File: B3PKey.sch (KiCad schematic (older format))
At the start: 4 parts

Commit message: Controller and keyswitch schematic
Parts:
- removed J?: USB_C_Receptacle, symbol Connector:USB_C_Receptacle
- added C?: 1uF, symbol Device:C_Small
- added C? (x3): 0.1uF, symbol Device:C_Small
- added C?: 10uF, symbol Device:C_Small
- added C? (x2): 22pF, symbol Device:C_Small
- added D? (x96): D_Small, symbol Device:D_Small
- added F?: 500mA, symbol Device:Polyfuse_Small
- added MX? (x96): MX-NoLED, symbol MX_Alps_Hybrid:MX-NoLED
- added R? (x2): 10k, symbol Device:R_Small
- added R? (x2): 22, symbol Device:R_Small
- added USB?: Molex-0548190589, symbol random-keyboard-parts:Molex-0548190589
- Y?: value Crystal_GND24_Small -> 16MHz
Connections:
- net D+: now also R?.2, USB?.3 (D+); no longer U?.4 (D+)
- net D-: now also R?.2, USB?.4 (D-); no longer U?.3 (D-)
- net at U?.13 (~RESET): now also SW?.2, R?.2
- net +5V: now reaches U?.14 (VCC), U?.34 (VCC)
- net +5V: now also U?.2 (UVCC), U?.24 (AVCC), U?.44 (AVCC), U?.7 (VBUS), C?.1, C?.1, C?.1, C?.1, F?.1, R?.1
- net GND: now reaches U?.15 (GND), U?.23 (GND), U?.35 (GND), U?.43 (GND)
- net GND: now also SW?.1, U?.5 (UGND), Y?.2, Y?.4, C?.2, C?.2, C?.2, C?.2, C?.2, C?.2, C?.2, R?.1, USB?.1 (GND)
- net at U?.16 (XTAL2): now also Y?.3, C?.1
- net at U?.17 (XTAL1): now also Y?.1, C?.1
- net at U?.33 (~HWB~/PE2): now also R?.2
- net at U?.6 (UCAP): now also C?.1
- new net: R?.1, U?.3 (D-)
- new net: R?.1, U?.4 (D+)
- new net: D?.2 (A), MX?.2 (ROW) (x96)
- new net COL0: MX?.1 (COL), MX?.1 (COL), MX?.1 (COL), MX?.1 (COL), MX?.1 (COL), MX?.1 (COL), MX?.1 (COL), MX?.1 (COL), MX?.1 (COL), MX?.1 (COL), MX?.1 (COL), MX?.1 (COL)
- new net COL1: MX?.1 (COL), MX?.1 (COL), MX?.1 (COL), MX?.1 (COL), MX?.1 (COL), MX?.1 (COL), MX?.1 (COL), MX?.1 (COL), MX?.1 (COL), MX?.1 (COL), MX?.1 (COL), MX?.1 (COL)
- new net COL2: MX?.1 (COL), MX?.1 (COL), MX?.1 (COL), MX?.1 (COL), MX?.1 (COL), MX?.1 (COL), MX?.1 (COL), MX?.1 (COL), MX?.1 (COL), MX?.1 (COL), MX?.1 (COL), MX?.1 (COL)
- new net COL3: MX?.1 (COL), MX?.1 (COL), MX?.1 (COL), MX?.1 (COL), MX?.1 (COL), MX?.1 (COL), MX?.1 (COL), MX?.1 (COL), MX?.1 (COL), MX?.1 (COL), MX?.1 (COL), MX?.1 (COL)
- new net COL4: MX?.1 (COL), MX?.1 (COL), MX?.1 (COL), MX?.1 (COL), MX?.1 (COL), MX?.1 (COL), MX?.1 (COL), MX?.1 (COL), MX?.1 (COL), MX?.1 (COL), MX?.1 (COL), MX?.1 (COL)
- new net COL5: MX?.1 (COL), MX?.1 (COL), MX?.1 (COL), MX?.1 (COL), MX?.1 (COL), MX?.1 (COL), MX?.1 (COL), MX?.1 (COL), MX?.1 (COL), MX?.1 (COL), MX?.1 (COL), MX?.1 (COL)
- new net COL6: MX?.1 (COL), MX?.1 (COL), MX?.1 (COL), MX?.1 (COL), MX?.1 (COL), MX?.1 (COL), MX?.1 (COL), MX?.1 (COL), MX?.1 (COL), MX?.1 (COL), MX?.1 (COL), MX?.1 (COL)
- new net COL7: MX?.1 (COL), MX?.1 (COL), MX?.1 (COL), MX?.1 (COL), MX?.1 (COL), MX?.1 (COL), MX?.1 (COL), MX?.1 (COL), MX?.1 (COL), MX?.1 (COL), MX?.1 (COL), MX?.1 (COL)
- new net ROW0: D?.1 (K), D?.1 (K), D?.1 (K), D?.1 (K), D?.1 (K), D?.1 (K), D?.1 (K), D?.1 (K)
- new net ROW1: D?.1 (K), D?.1 (K), D?.1 (K), D?.1 (K), D?.1 (K), D?.1 (K), D?.1 (K), D?.1 (K)
- new net ROW10: D?.1 (K), D?.1 (K), D?.1 (K), D?.1 (K), D?.1 (K), D?.1 (K), D?.1 (K), D?.1 (K)
- new net ROW11: D?.1 (K), D?.1 (K), D?.1 (K), D?.1 (K), D?.1 (K), D?.1 (K), D?.1 (K), D?.1 (K)
- new net ROW2: D?.1 (K), D?.1 (K), D?.1 (K), D?.1 (K), D?.1 (K), D?.1 (K), D?.1 (K), D?.1 (K)
- new net ROW3: D?.1 (K), D?.1 (K), D?.1 (K), D?.1 (K), D?.1 (K), D?.1 (K), D?.1 (K), D?.1 (K)
- new net ROW4: D?.1 (K), D?.1 (K), D?.1 (K), D?.1 (K), D?.1 (K), D?.1 (K), D?.1 (K), D?.1 (K)
- new net ROW5: D?.1 (K), D?.1 (K), D?.1 (K), D?.1 (K), D?.1 (K), D?.1 (K), D?.1 (K), D?.1 (K)
- new net ROW6: D?.1 (K), D?.1 (K), D?.1 (K), D?.1 (K), D?.1 (K), D?.1 (K), D?.1 (K), D?.1 (K)
- new net ROW7: D?.1 (K), D?.1 (K), D?.1 (K), D?.1 (K), D?.1 (K), D?.1 (K), D?.1 (K), D?.1 (K)
- new net ROW8: D?.1 (K), D?.1 (K), D?.1 (K), D?.1 (K), D?.1 (K), D?.1 (K), D?.1 (K), D?.1 (K)
- new net ROW9: D?.1 (K), D?.1 (K), D?.1 (K), D?.1 (K), D?.1 (K), D?.1 (K), D?.1 (K), D?.1 (K)
- new net VCC: F?.2, USB?.5 (VBUS)
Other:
- moved on the sheet: SW?, U?, Y?

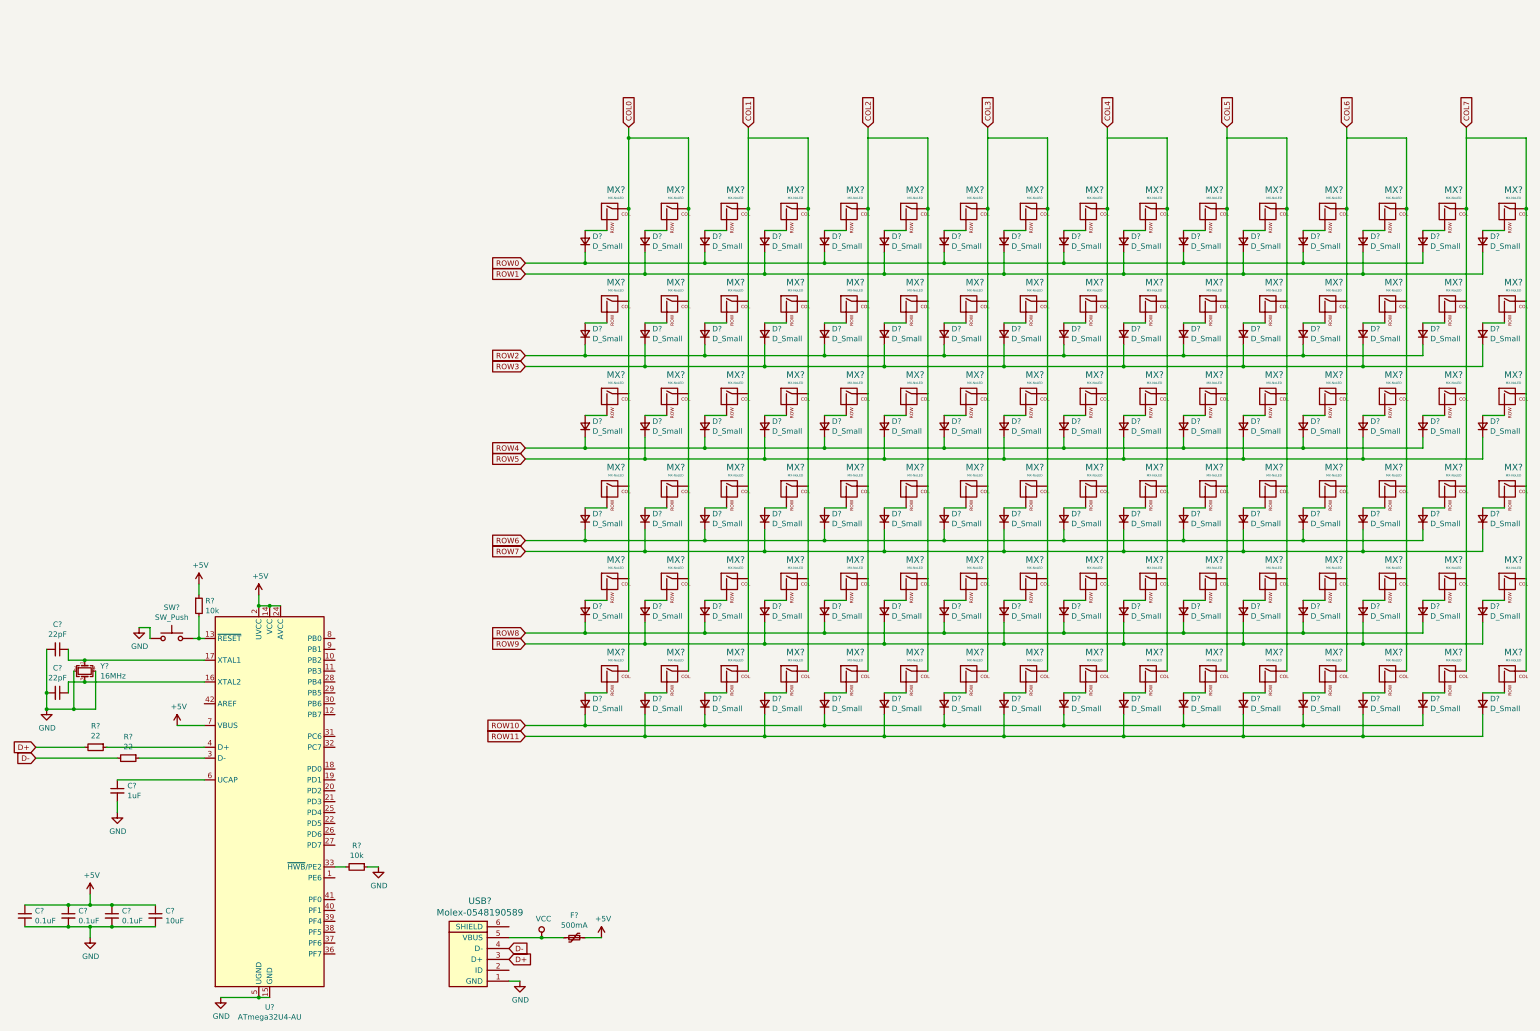
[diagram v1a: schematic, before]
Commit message: Updated switch matrix
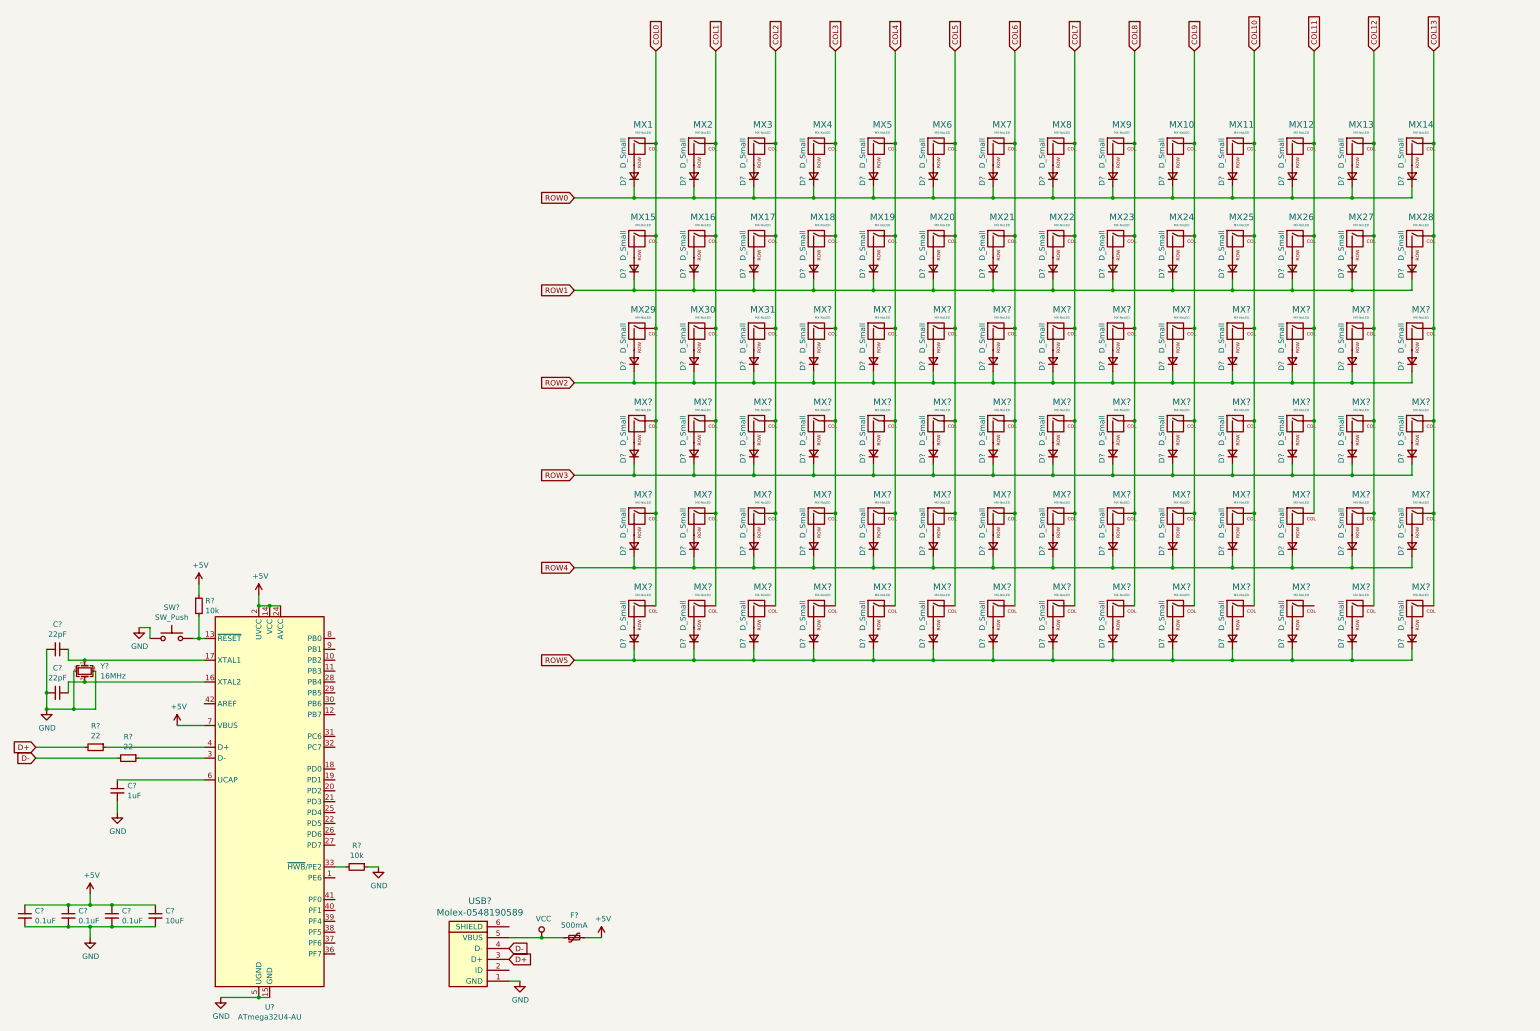
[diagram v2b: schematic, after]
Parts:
- removed D? (x95): D_Small, symbol Device:D_Small
- removed MX? (x95): MX-NoLED, symbol MX_Alps_Hybrid:MX-NoLED
- added D? (x83): D_Small, symbol Device:D_Small
- added MX10, MX11, MX12, MX13, MX14, MX15, MX16, MX17, MX18, MX19, MX2, MX20, MX21, MX22, MX23, MX24, MX25, MX26, MX27, MX28, MX29, MX3, MX30, MX31, MX4, MX5, MX6, MX7, MX8, MX9, MX? (x53): MX-NoLED, symbol MX_Alps_Hybrid:MX-NoLED
- gave numbers to parts that had none: 1
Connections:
- net COL0: now also MX15.1 (COL), MX29.1 (COL), MX?.1 (COL), MX?.1 (COL), MX?.1 (COL)
- net COL1: now also MX16.1 (COL), MX2.1 (COL), MX30.1 (COL), MX?.1 (COL), MX?.1 (COL), MX?.1 (COL)
- net COL2: now also MX17.1 (COL), MX3.1 (COL), MX31.1 (COL), MX?.1 (COL), MX?.1 (COL), MX?.1 (COL)
- net COL3: now also MX18.1 (COL), MX4.1 (COL), MX?.1 (COL), MX?.1 (COL), MX?.1 (COL), MX?.1 (COL)
- net COL4: now also MX19.1 (COL), MX5.1 (COL), MX?.1 (COL), MX?.1 (COL), MX?.1 (COL), MX?.1 (COL)
- net COL5: now also MX20.1 (COL), MX6.1 (COL), MX?.1 (COL), MX?.1 (COL), MX?.1 (COL), MX?.1 (COL)
- net COL6: now also MX21.1 (COL), MX7.1 (COL), MX?.1 (COL), MX?.1 (COL), MX?.1 (COL), MX?.1 (COL)
- net COL7: now also MX22.1 (COL), MX8.1 (COL), MX?.1 (COL), MX?.1 (COL), MX?.1 (COL), MX?.1 (COL)
- net ROW0: now also D?.1 (K), D?.1 (K), D?.1 (K), D?.1 (K), D?.1 (K), D?.1 (K), D?.1 (K), D?.1 (K), D?.1 (K), D?.1 (K), D?.1 (K), D?.1 (K), D?.1 (K)
- net ROW1: now also D?.1 (K), D?.1 (K), D?.1 (K), D?.1 (K), D?.1 (K), D?.1 (K), D?.1 (K), D?.1 (K), D?.1 (K), D?.1 (K), D?.1 (K), D?.1 (K), D?.1 (K), D?.1 (K)
- net ROW2: now also D?.1 (K), D?.1 (K), D?.1 (K), D?.1 (K), D?.1 (K), D?.1 (K), D?.1 (K), D?.1 (K), D?.1 (K), D?.1 (K), D?.1 (K), D?.1 (K), D?.1 (K), D?.1 (K)
- net ROW3: now also D?.1 (K), D?.1 (K), D?.1 (K), D?.1 (K), D?.1 (K), D?.1 (K), D?.1 (K), D?.1 (K), D?.1 (K), D?.1 (K), D?.1 (K), D?.1 (K), D?.1 (K), D?.1 (K)
- net ROW4: now also D?.1 (K), D?.1 (K), D?.1 (K), D?.1 (K), D?.1 (K), D?.1 (K), D?.1 (K), D?.1 (K), D?.1 (K), D?.1 (K), D?.1 (K), D?.1 (K), D?.1 (K), D?.1 (K)
- net ROW5: now also D?.1 (K), D?.1 (K), D?.1 (K), D?.1 (K), D?.1 (K), D?.1 (K), D?.1 (K), D?.1 (K), D?.1 (K), D?.1 (K), D?.1 (K), D?.1 (K), D?.1 (K), D?.1 (K)
- new net: D?.2 (A), MX2.2 (ROW)
- new net: D?.2 (A), MX3.2 (ROW)
- new net: D?.2 (A), MX4.2 (ROW)
- new net: D?.2 (A), MX5.2 (ROW)
- new net: D?.2 (A), MX6.2 (ROW)
- new net: D?.2 (A), MX7.2 (ROW)
- new net: D?.2 (A), MX8.2 (ROW)
- new net: D?.2 (A), MX9.2 (ROW)
- new net: D?.2 (A), MX10.2 (ROW)
- new net: D?.2 (A), MX11.2 (ROW)
- new net: D?.2 (A), MX12.2 (ROW)
- new net: D?.2 (A), MX13.2 (ROW)
- new net: D?.2 (A), MX14.2 (ROW)
- new net: D?.2 (A), MX15.2 (ROW)
- new net: D?.2 (A), MX16.2 (ROW)
- new net: D?.2 (A), MX17.2 (ROW)
- new net: D?.2 (A), MX18.2 (ROW)
- new net: D?.2 (A), MX19.2 (ROW)
- new net: D?.2 (A), MX20.2 (ROW)
- new net: D?.2 (A), MX21.2 (ROW)
- new net: D?.2 (A), MX22.2 (ROW)
- new net: D?.2 (A), MX23.2 (ROW)
- new net: D?.2 (A), MX24.2 (ROW)
- new net: D?.2 (A), MX25.2 (ROW)
- new net: D?.2 (A), MX26.2 (ROW)
- new net: D?.2 (A), MX27.2 (ROW)
- new net: D?.2 (A), MX28.2 (ROW)
- new net: D?.2 (A), MX29.2 (ROW)
- new net: D?.2 (A), MX30.2 (ROW)
- new net: D?.2 (A), MX31.2 (ROW)
- new net: D?.2 (A), MX?.2 (ROW) (x53)
- new net COL10: MX11.1 (COL), MX25.1 (COL), MX?.1 (COL), MX?.1 (COL), MX?.1 (COL), MX?.1 (COL)
- new net COL11: MX12.1 (COL), MX26.1 (COL), MX?.1 (COL), MX?.1 (COL), MX?.1 (COL)
- new net COL12: MX13.1 (COL), MX27.1 (COL), MX?.1 (COL), MX?.1 (COL), MX?.1 (COL), MX?.1 (COL)
- new net COL13: MX14.1 (COL), MX28.1 (COL), MX?.1 (COL), MX?.1 (COL), MX?.1 (COL), MX?.1 (COL)
- new net COL8: MX23.1 (COL), MX9.1 (COL), MX?.1 (COL), MX?.1 (COL), MX?.1 (COL), MX?.1 (COL)
- new net COL9: MX10.1 (COL), MX24.1 (COL), MX?.1 (COL), MX?.1 (COL), MX?.1 (COL), MX?.1 (COL)
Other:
- moved on the sheet: D?, MX1

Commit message: Keyswitch layout w/ diodes
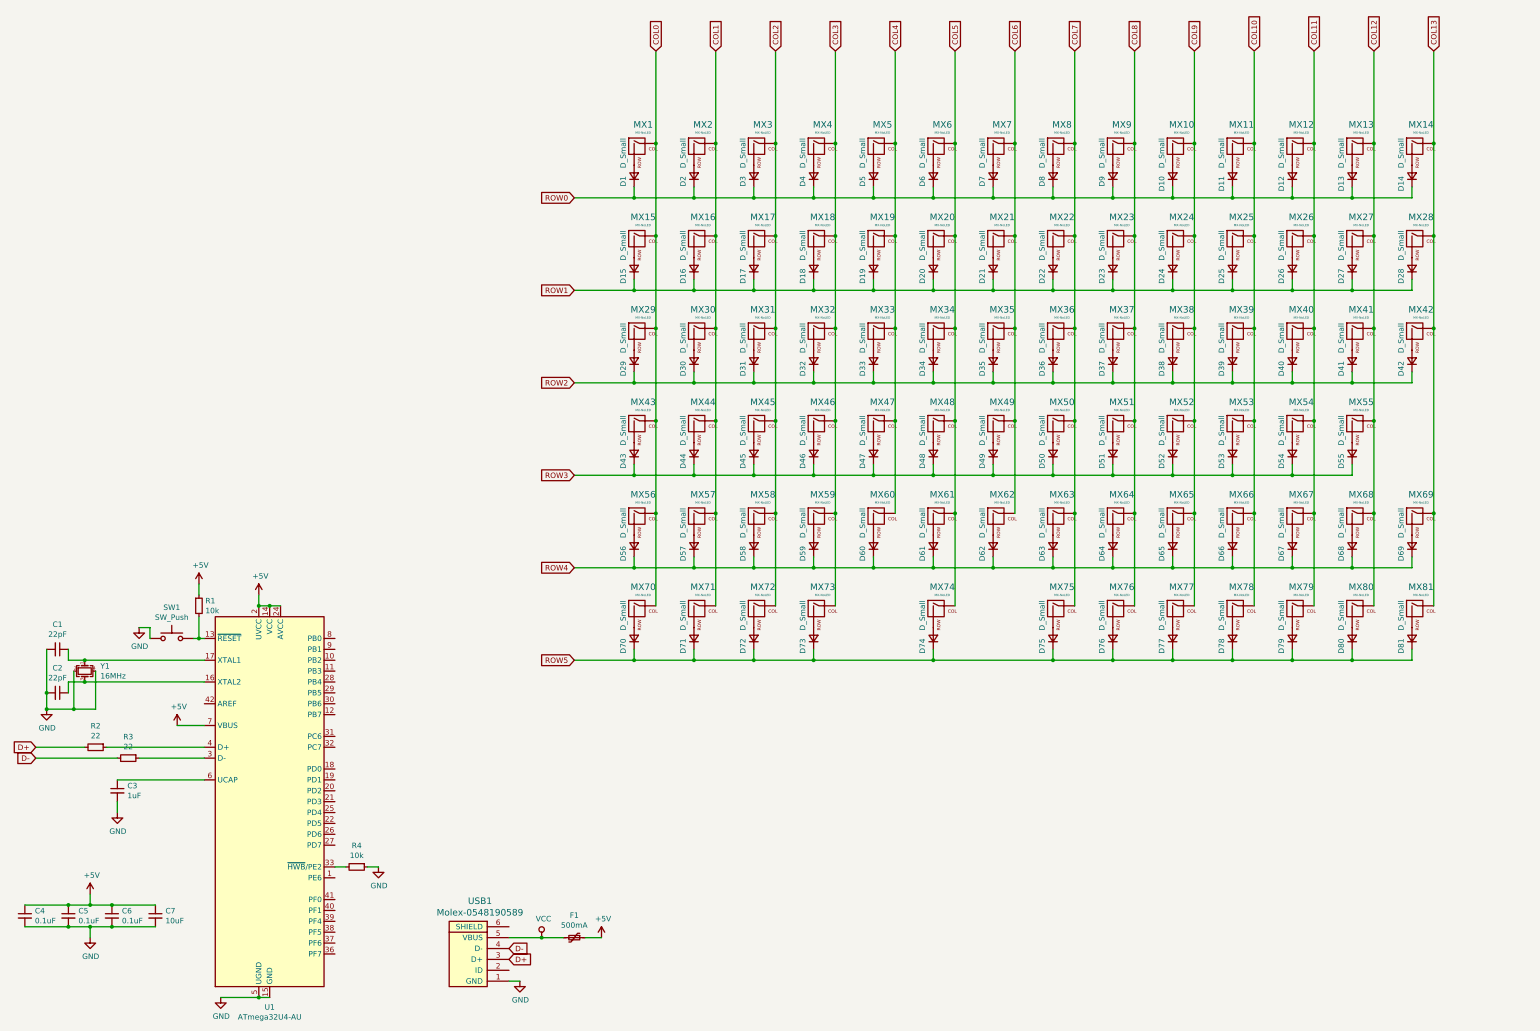
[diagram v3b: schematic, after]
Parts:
- removed D? (x4): D_Small, symbol Device:D_Small
- removed MX? (x4): MX-NoLED, symbol MX_Alps_Hybrid:MX-NoLED
- added D81: D_Small, Diode_SMD:D_SOD-123, symbol Device:D_Small
- added MX81: MX-NoLED, MX_Only:MXOnly-1U-NoLED, symbol MX_Alps_Hybrid:MX-NoLED
- C1, C2, C3, C4, C5, C6, C7: renamed from C?; footprint (none) -> Capacitor_SMD:C_0805_2012Metric
- D1, D10, D11, D12, D13, D14, D15, D16, D17, D18, D19, D2, D20, D21, D22, D23, D24, D25, D26, D27, D28, D29, D3, D30, D31, D32, D33, D34, D35, D36, D37, D38, D39, D4, D40, D41, D42, D43, D44, D45, D46, D47, D48, D49, D5, D50, D51, D52, D53, D54, D55, D56, D57, D58, D59, D6, D60, D61, D62, D63, D64, D65, D66, D67, D68, D69, D7, D70, D71, D72, D73, D74, D75, D76, D77, D78, D79, D8, D80, D9: renamed from D?; footprint (none) -> Diode_SMD:D_SOD-123
- F1: renamed from F?; footprint (none) -> Fuse:Fuse_0805_2012Metric
- MX1, MX10, MX11, MX12, MX13, MX14, MX15, MX16, MX17, MX18, MX19, MX2, MX20, MX21, MX22, MX23, MX24, MX25, MX26, MX27, MX28, MX29, MX3, MX30, MX31, MX4, MX5, MX6, MX7, MX8, MX9: footprint (none) -> MX_Only:MXOnly-1U-NoLED
- MX32, MX33, MX34, MX35, MX36, MX37, MX38, MX39, MX40, MX41, MX42, MX43, MX44, MX45, MX46, MX47, MX48, MX49, MX50, MX51, MX52, MX53, MX54, MX56, MX57, MX58, MX59, MX60, MX61, MX62, MX63, MX64, MX65, MX66, MX67, MX68, MX69, MX70, MX71, MX72, MX73, MX75, MX76, MX77, MX78, MX79, MX80: renamed from MX?; footprint (none) -> MX_Only:MXOnly-1U-NoLED
- MX55: renamed from MX?; footprint (none) -> MX_Only:MXOnly-2U-NoLED
- MX74: renamed from MX?; footprint (none) -> MX_Only:MXOnly-3U-NoLED
- R1, R2, R3, R4: renamed from R?; footprint (none) -> Resistor_SMD:R_0805_2012Metric
- SW1: renamed from SW?; footprint (none) -> random-keyboard-parts:SKQG-1155865
- USB1: renamed from USB?; footprint (none) -> random-keyboard-parts:Molex-0548190589
- Y1: renamed from Y?; footprint (none) -> Crystal:Crystal_SMD_3225-4Pin_3.2x2.5mm
- gave numbers to parts that had none: 1
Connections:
- net COL10: now also MX78.1 (COL); no longer MX80.1 (COL)
- net COL11: now also MX79.1 (COL)
- net COL12: now also MX80.1 (COL)
- net COL13: now also MX81.1 (COL)
- net COL4: no longer MX74.1 (COL)
- net COL5: now also MX74.1 (COL); no longer MX75.1 (COL)
- net COL6: no longer MX76.1 (COL)
- net COL7: now also MX75.1 (COL); no longer MX77.1 (COL)
- net COL8: now also MX76.1 (COL); no longer MX78.1 (COL)
- net COL9: now also MX77.1 (COL); no longer MX79.1 (COL)
- net ROW5: now also D81.1 (K)
- new net: D81.2 (A), MX81.2 (ROW)
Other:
- moved on the sheet: D74, D75, D76, D77, D78, D79, D80, MX74, MX75, MX76, MX77, MX78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

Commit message: Flip spacebar stabs
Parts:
- MX74: footprint MX_Only:MXOnly-3U-NoLED -> MX_Only:MXOnly-3U-ReversedStabilizers-NoLED
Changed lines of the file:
@@
 F 0 "MX74" H 9283 7473 60  0000 C CNN
 F 1 "MX-NoLED" H 9283 7399 20  0000 C CNN
-F 2 "MX_Only:MXOnly-3U-NoLED" H 8625 7225 60  0001 C CNN
+F 2 "MX_Only:MXOnly-3U-ReversedStabilizers-NoLED" H 8625 7225 60  0001 C CNN
 F 3 "" H 8625 7225 60  0001 C CNN
 	1    9250 7250
